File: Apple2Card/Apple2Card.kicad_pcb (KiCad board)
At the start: 2 copper layers, 160 x 78.2 mm, 55 parts, among them J1 ICSP, J2 Conn_01x25, J3 Conn_01x25, J4 Conn_01x16, J5 Conn_01x04, J6 WIZNET 5500, J7 Conn_01x04, SW1 SW_Push, U1 ATmega328P-P, U3 74HCT00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

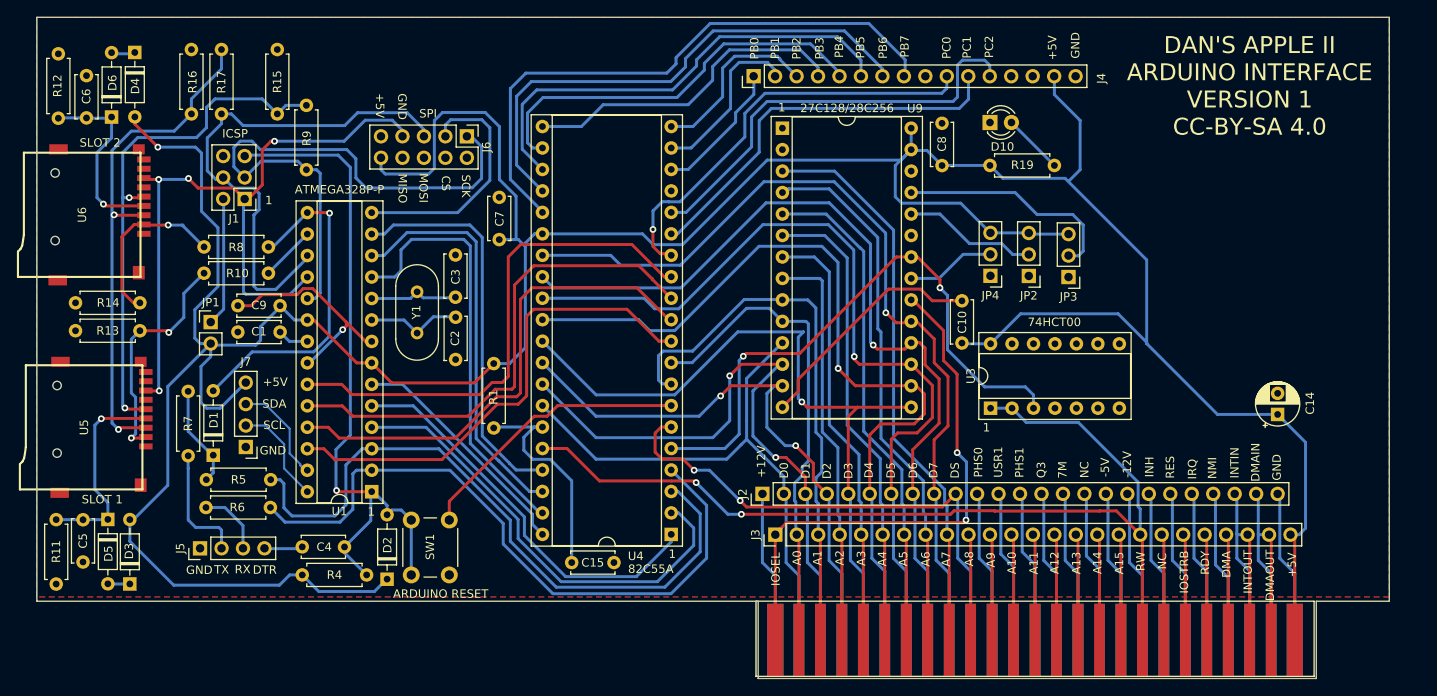
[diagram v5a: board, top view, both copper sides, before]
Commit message: Added ROM banking
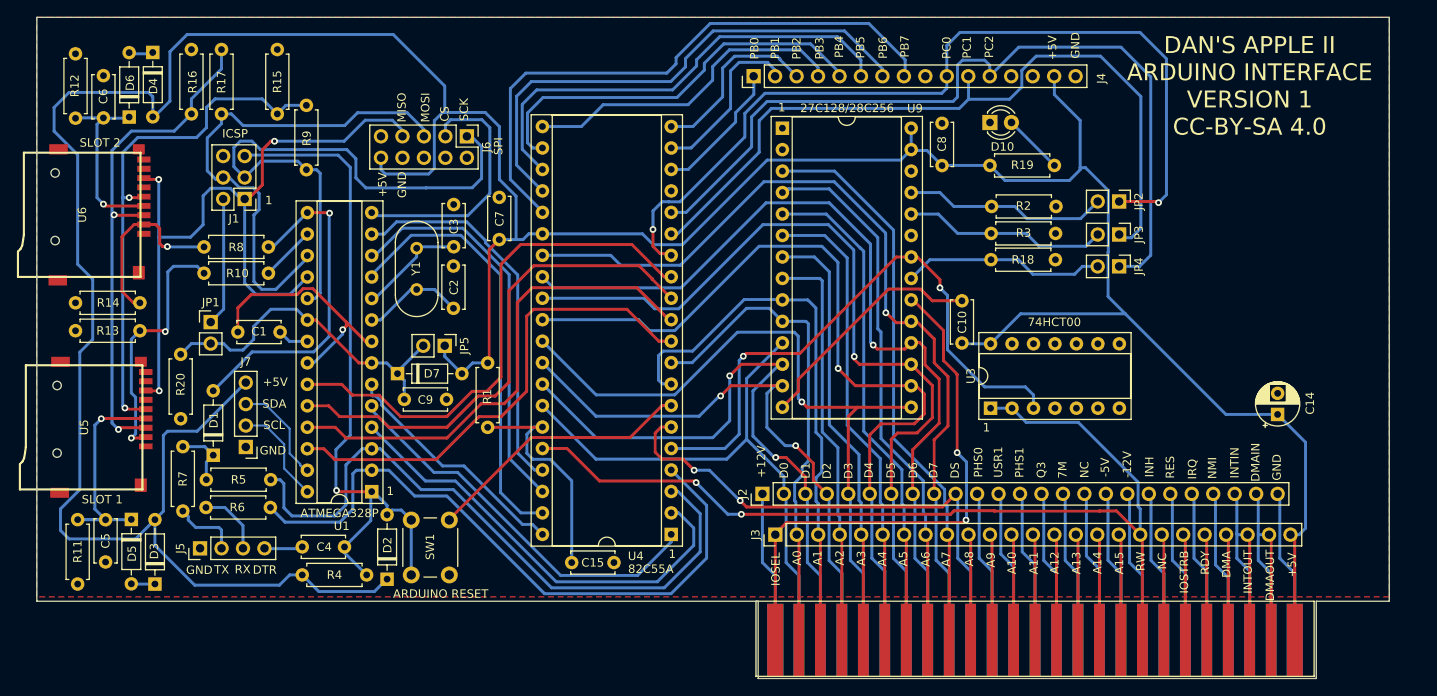
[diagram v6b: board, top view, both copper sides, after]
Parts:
- added D7: 1N4148, Diode_THT:D_DO-35_SOD27_P7.62mm_Horizontal, F.Cu at (75.7, 67.6)
- added JP5: PWR, Connector_PinHeader_2.54mm:PinHeader_1x02_P2.54mm_Vertical, F.Cu at (81.3, 64.3)
- added R18: 10k, Resistor_THT:R_Axial_DIN0207_L6.3mm_D2.5mm_P7.62mm_Horizontal, F.Cu at (145.9, 54.1)
- added R2: 10k, Resistor_THT:R_Axial_DIN0207_L6.3mm_D2.5mm_P7.62mm_Horizontal, F.Cu at (146.0, 47.8)
- added R20: 10k, Resistor_THT:R_Axial_DIN0207_L6.3mm_D2.5mm_P7.62mm_Horizontal, F.Cu at (50.0, 72.9)
- added R3: 10k, Resistor_THT:R_Axial_DIN0207_L6.3mm_D2.5mm_P7.62mm_Horizontal, F.Cu at (145.9, 51.0)
- JP2: value RS1 -> PG0; footprint Connector_PinHeader_2.54mm:PinHeader_1x03_P2.54mm_Vertical -> Connector_PinHeader_2.54mm:PinHeader_1x02_P2.54mm_Vertical
- JP3: value RS0 -> PG1; footprint Connector_PinHeader_2.54mm:PinHeader_1x03_P2.54mm_Vertical -> Connector_PinHeader_2.54mm:PinHeader_1x02_P2.54mm_Vertical
- JP4: value RS2 -> PG2; footprint Connector_PinHeader_2.54mm:PinHeader_1x03_P2.54mm_Vertical -> Connector_PinHeader_2.54mm:PinHeader_1x02_P2.54mm_Vertical
- moved C9 18.4 mm to (76.5, 70.6), turned to 0 degrees
- moved JP4 15.3 mm to (161.1, 54.9), turned to -90 degrees
- moved JP2 13.9 mm to (161.1, 47.2), turned to -90 degrees
- moved JP3 7.83 mm to (161.1, 51.1), turned to -90 degrees
- moved R7 6.57 mm to (50.3, 83.8)
- moved C3 5.97 mm to (82.3, 52.5)
- moved Y1 5.16 mm to (78.0, 52.7)
- moved D3 2.97 mm to (47.0, 92.5)
- moved D5 2.78 mm to (44.2, 84.8)
- moved C5 2.67 mm to (41.1, 84.8)
- moved R11 2.54 mm to (37.8, 92.5)
- moved D4 2.13 mm to (46.7, 29.6)
- moved D6 2.08 mm to (43.9, 37.2)
- moved R12 2.03 mm to (37.6, 29.7)
- moved C6 2.00 mm to (40.9, 37.3)
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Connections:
- C9 pad 1: +5V -> Net-(U1-Pad20)
- J4 pad 10: Net-(J4-Pad10) -> PC0
- J4 pad 11: Net-(J4-Pad11) -> PC1
- J4 pad 12: Net-(J4-Pad12) -> PC2
- JP1 pad 2: +5V -> Net-(U1-Pad20)
- JP2 pad 1: GND -> PC0
- JP2 pad 2: Net-(JP2-Pad2) -> Net-(U9-Pad25)
- JP3 pad 1: GND -> PC1
- JP3 pad 2: Net-(JP3-Pad2) -> Net-(U9-Pad24)
- JP4 pad 1: GND -> PC2
- U1 pad 20: +5V -> Net-(U1-Pad20)
- U1 pad 7: +5V -> Net-(U1-Pad20)
- U4 pad 14: Net-(J4-Pad10) -> PC0
- U4 pad 15: Net-(J4-Pad11) -> PC1
- U4 pad 16: Net-(J4-Pad12) -> PC2
- U9 pad 24: Net-(JP2-Pad2) -> Net-(U9-Pad24)
- U9 pad 25: Net-(JP3-Pad2) -> Net-(U9-Pad25)
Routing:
- net PC0: track 0.00 -> 104.3 mm, vias 0 -> 2
- net PC2: track 0.00 -> 98.3 mm
- net PC1: track 0.00 -> 91.1 mm
- net Net-(J4-Pad12): track 51.0 -> 0.00 mm
- net Net-(J4-Pad10): track 50.6 -> 0.00 mm, vias 1 -> 0
- net Net-(J4-Pad11): track 46.7 -> 0.00 mm
- net Net-(U1-Pad20): track 0.00 -> 40.5 mm
- net Net-(JP3-Pad2): track 27.0 -> 0.00 mm
- net Net-(U9-Pad24): track 0.00 -> 24.2 mm
- net Net-(U9-Pad25): track 0.00 -> 24.2 mm
- net Net-(JP2-Pad2): track 15.9 -> 0.00 mm
- net Net-(U9-Pad21): track 10.6 -> 24.1 mm
- net Net-(J5-Pad2): track 14.2 -> 7.92 mm
- net +5V: track 423.9 -> 430.0 mm, vias 1 -> 0
- net Net-(D1-Pad1): track 12.1 -> 7.26 mm
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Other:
- board text added: "ATMEGA328P"
- board text removed: "ATMEGA328P-P"

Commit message: Before combining connectors
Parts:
- moved D3 2.61 mm to (44.4, 92.4)
- moved D5 2.41 mm to (41.8, 84.8)
- moved C5 2.27 mm to (38.9, 84.7)
- moved R11 2.10 mm to (35.8, 92.4)
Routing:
- net +5V: track 430.0 -> 433.0 mm
- net A7: track 67.3 -> 68.7 mm
- net D7: track 102.0 -> 103.1 mm
- net A6: track 63.9 -> 64.6 mm
- net D6: track 101.8 -> 102.5 mm
- net A0: track 57.9 -> 57.3 mm
- net A5: track 59.5 -> 60.1 mm

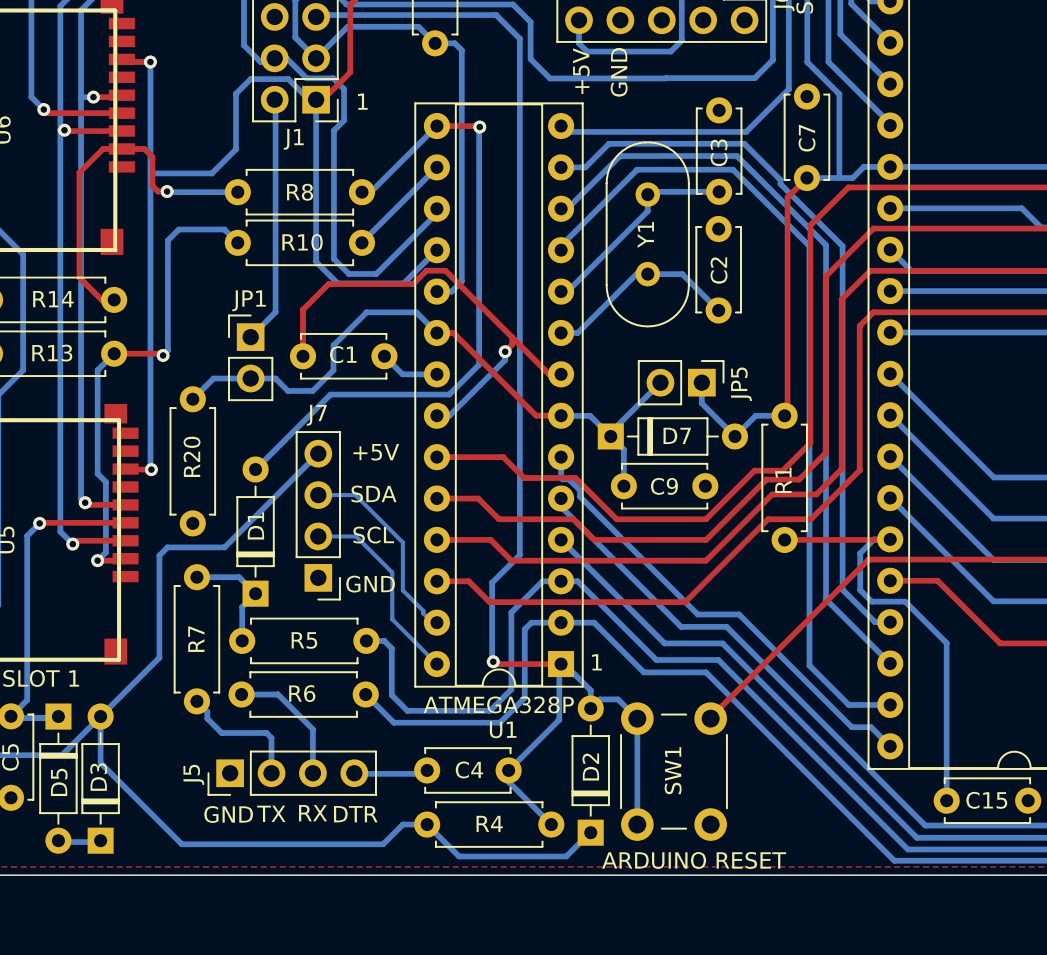
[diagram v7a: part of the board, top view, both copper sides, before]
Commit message: Added initial boot firmware
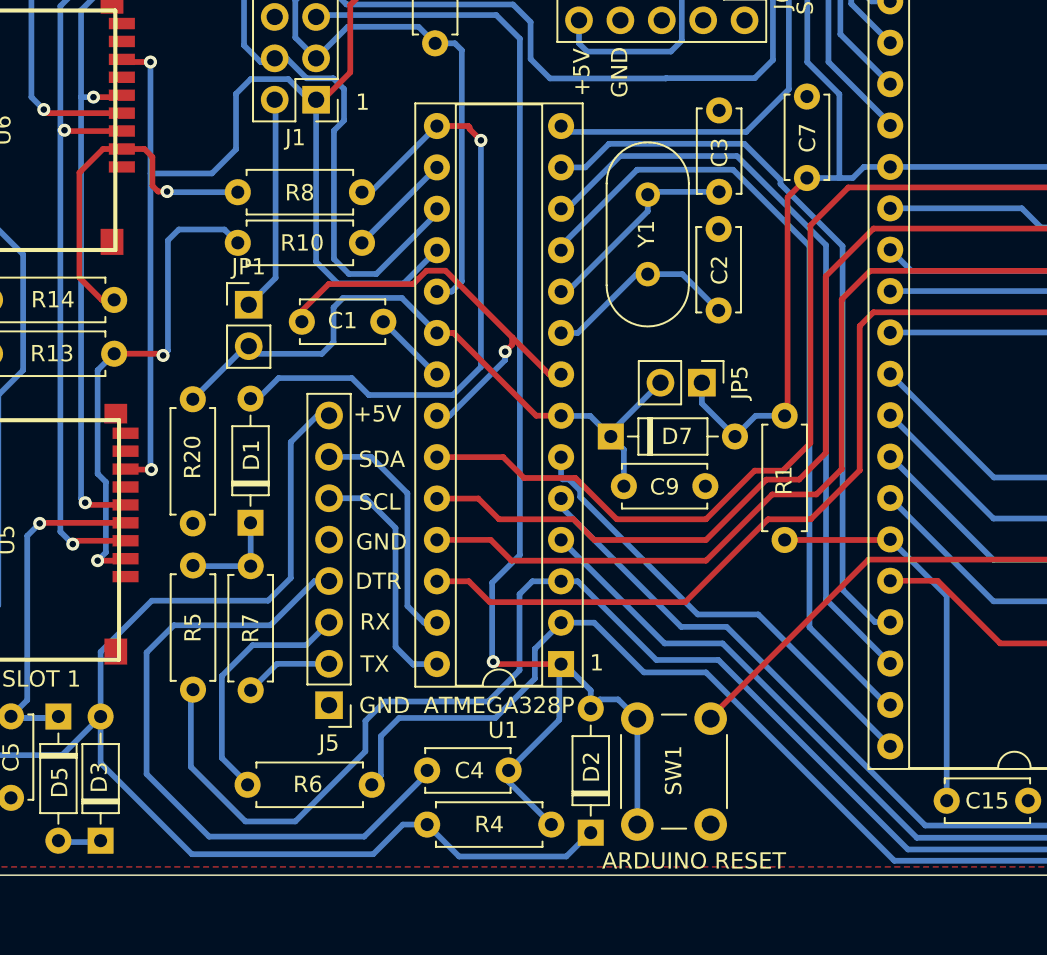
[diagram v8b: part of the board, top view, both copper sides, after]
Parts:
- removed J7: Conn_01x04, Connector_PinHeader_2.54mm:PinHeader_1x04_P2.54mm_Vertical
- J5: value Conn_01x04 -> Conn_01x08; footprint Connector_PinHeader_2.54mm:PinHeader_1x04_P2.54mm_Vertical -> Connector_PinHeader_2.54mm:PinHeader_1x08_P2.54mm_Vertical
- moved J5 7.37 mm to (58.4, 84.1), turned to 180 degrees
- moved R6 5.55 mm to (53.4, 88.9)
- moved R5 5.53 mm to (50.0, 75.5), turned to -90 degrees
- moved D1 4.36 mm to (53.6, 72.9)
- moved R7 3.37 mm to (53.6, 83.1)
- moved C1 2.12 mm to (61.7, 60.5)
- moved JP1 1.99 mm to (53.5, 59.5)
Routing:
- net Net-(C4-Pad1): track 4.57 -> 41.1 mm
- net PD1: track 78.0 -> 95.3 mm
- net Net-(J5-Pad3): track 7.96 -> 15.3 mm
- net +5V: track 433.0 -> 438.6 mm
- net Net-(C15-Pad1): track 27.3 -> 24.0 mm
- net PC5: track 12.2 -> 15.1 mm
- net PC4: track 12.3 -> 14.9 mm
- net Net-(J5-Pad2): track 7.92 -> 5.48 mm
- net GND: track 108.0 -> 105.9 mm
- net Net-(J1-Pad2): track 15.2 -> 13.3 mm
- net PD5: track 51.1 -> 49.7 mm
- net Net-(D1-Pad1): track 7.26 -> 6.22 mm
- net Net-(C1-Pad1): track 3.68 -> 4.63 mm
- net Net-(C9-Pad1): track 40.5 -> 41.3 mm
- net CS2: track 39.9 -> 39.1 mm
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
